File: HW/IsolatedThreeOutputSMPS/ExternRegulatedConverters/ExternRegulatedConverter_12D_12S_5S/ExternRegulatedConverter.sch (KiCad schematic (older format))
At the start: 21 parts, among them J1 15VDC, J2 Conn_01x07, U1 RS6-1212D, U2 LM7805_TO220, U3 LM7812_TO220, U4 LM7912_TO220, U5 LM7812_TO220

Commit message: updated hw
- finished layout for power supply
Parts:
- removed L1: 10mH, Inductor_THT:Choke_Schaffner_RN204-04-9.0x14.0mm, symbol Device:L_Core_Iron_Coupled
- C11: value 1uF -> 10uF
- C2, C5: value 200nF -> 330nF
- C3, C4: footprint Capacitor_SMD:C_0805_2012Metric_Pad1.15x1.40mm_HandSolder -> Capacitor_SMD:C_1206_3216Metric_Pad1.42x1.75mm_HandSolder
- C7: value 220nF -> 330nF
- C8: value 2.2uF -> 10uF
- J1: footprint Connector_PinHeader_2.54mm:PinHeader_1x02_P2.54mm_Vertical -> Connector_Molex:Molex_KK-254_AE-6410-02A_1x02_P2.54mm_Vertical
- J2: footprint (none) -> Connector_Molex:Molex_KK-254_AE-6410-07A_1x07_P2.54mm_Vertical
- U1: symbol DCConverters:RS6-1212D -> ExternRegulatedConverter-rescue:RS6-1212D-DCConverters
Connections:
- net labels added: +12P, +15V
- net labels removed: VDD
- wire segments 110 -> 104
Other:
- moved on the sheet: C1, C10, C11, C2, C3, C4, C5, C6, C7, C8, C9, D1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

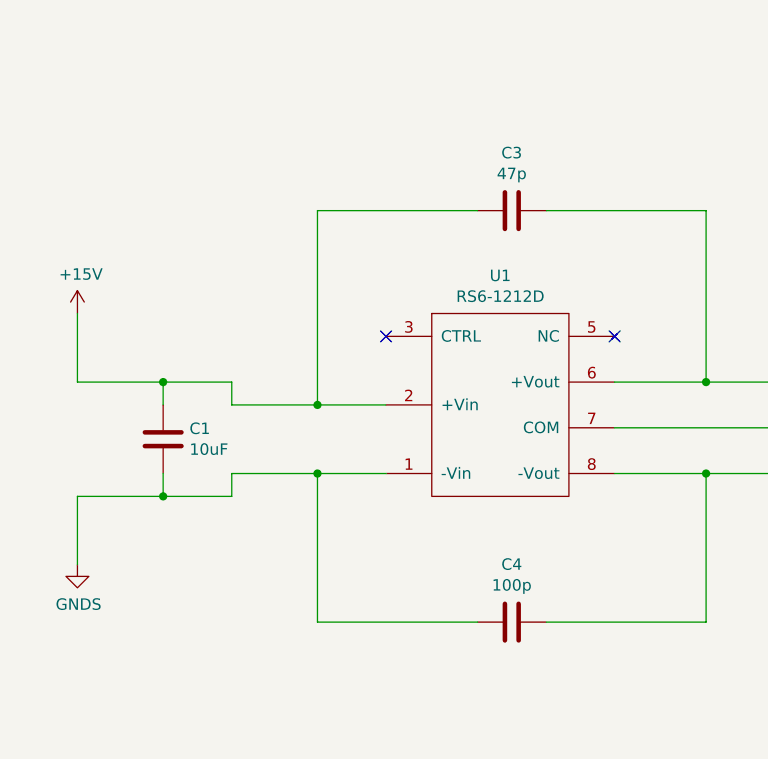
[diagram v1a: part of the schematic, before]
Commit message: updated HW
- ExternRegulatedConverter_12D_12S_5S layout optimised for etching
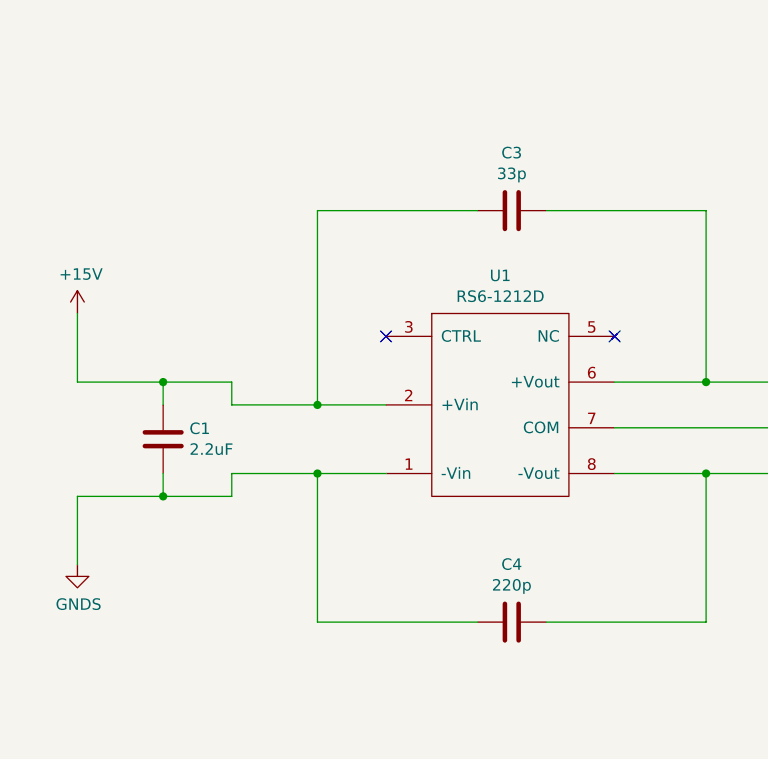
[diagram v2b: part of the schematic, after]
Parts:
- C1: value 10uF -> 2.2uF
- C3: value 47p -> 33p
- C4: value 100p -> 220p
- D1: footprint Diode_SMD:D_SMA-SMB_Universal_Handsoldering -> Diode_SMD:D_SMA_Handsoldering
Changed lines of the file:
@@
 P 3325 3425
 F 0 "C3" V 3073 3425 50  0000 C CNN
-F 1 "47p" V 3164 3425 50  0000 C CNN
+F 1 "33p" V 3164 3425 50  0000 C CNN
 F 2 "Capacitor_SMD:C_1206_3216Metric_Pad1.42x1.75mm_HandSolder" H 3363 3275 50  0001 C CNN
 F 3 "~" H 3325 3425 50  0001 C CNN
@@
 P 3325 5225
 F 0 "C4" V 3073 5225 50  0000 C CNN
-F 1 "100p" V 3164 5225 50  0000 C CNN
+F 1 "220p" V 3164 5225 50  0000 C CNN
 F 2 "Capacitor_SMD:C_1206_3216Metric_Pad1.42x1.75mm_HandSolder" H 3363 5075 50  0001 C CNN
 F 3 "~" H 3325 5225 50  0001 C CNN
@@
 P 1800 4425
 F 0 "C1" H 1915 4471 50  0000 L CNN
-F 1 "10uF" H 1915 4380 50  0000 L CNN
+F 1 "2.2uF" H 1915 4380 50  0000 L CNN
 F 2 "Capacitor_SMD:CP_Elec_4x5.7" H 1838 4275 50  0001 C CNN
 F 3 "~" H 1800 4425 50  0001 C CNN
@@
 F 0 "D1" H 1925 1609 50  0000 C CNN
 F 1 "D_Schottky" H 1925 1700 50  0000 C CNN
-F 2 "Diode_SMD:D_SMA-SMB_Universal_Handsoldering" H 1925 1825 50  0001 C CNN
+F 2 "Diode_SMD:D_SMA_Handsoldering" H 1925 1825 50  0001 C CNN
 F 3 "~" H 1925 1825 50  0001 C CNN
 	1    1925 1825

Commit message: added front panel design
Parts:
- U2: symbol Regulator_Linear:LM7805_TO220 -> ExternRegulatedConverter-rescue:LM7805_TO220-Regulator_Linear
- U3, U5: symbol Regulator_Linear:LM7812_TO220 -> ExternRegulatedConverter-rescue:LM7812_TO220-Regulator_Linear
- U4: symbol Regulator_Linear:LM7912_TO220 -> ExternRegulatedConverter-rescue:LM7912_TO220-Regulator_Linear
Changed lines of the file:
@@
 $EndComp
 $Comp
-L Regulator_Linear:LM7912_TO220 U4
+L ExternRegulatedConverter-rescue:LM7912_TO220-Regulator_Linear U4
 U 1 1 5CFB7C7C
 P 5525 4875
@@
 $EndComp
 $Comp
-L Regulator_Linear:LM7812_TO220 U3
+L ExternRegulatedConverter-rescue:LM7812_TO220-Regulator_Linear U3
 U 1 1 5CFB7D75
 P 5525 3875
@@
 	2075 1825 2375 1825
 $Comp
-L Regulator_Linear:LM7805_TO220 U2
+L ExternRegulatedConverter-rescue:LM7805_TO220-Regulator_Linear U2
 U 1 1 5D0A57CB
 P 4200 8225
@@
 Connection ~ 4200 7225
 $Comp
-L Regulator_Linear:LM7812_TO220 U5
+L ExternRegulatedConverter-rescue:LM7812_TO220-Regulator_Linear U5
 U 1 1 5D121B10
 P 4200 6525
